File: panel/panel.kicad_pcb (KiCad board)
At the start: 2 copper layers, 80.9 x 128.5 mm, 4 parts

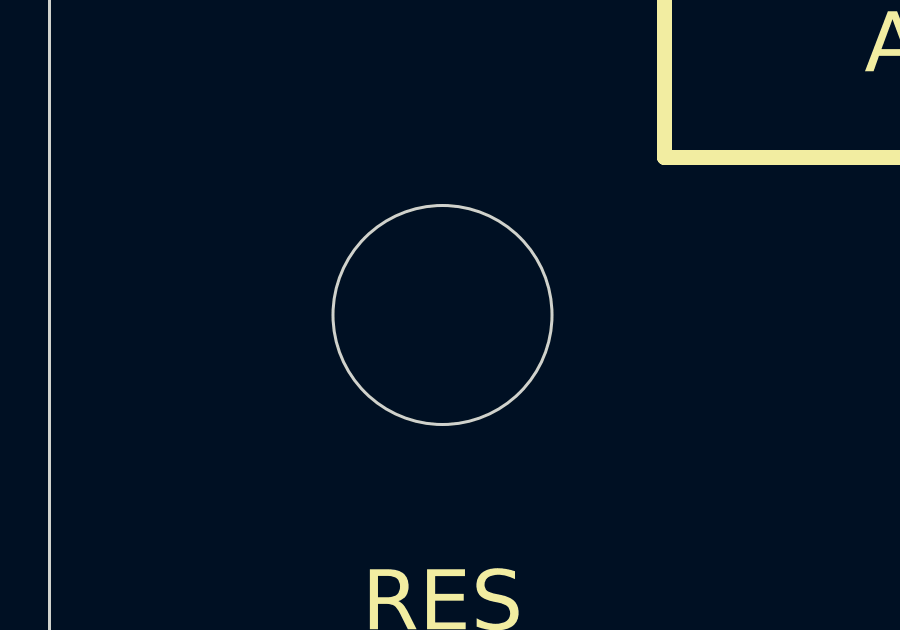
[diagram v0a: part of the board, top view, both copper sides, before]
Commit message: Added negative voltage protection diodes
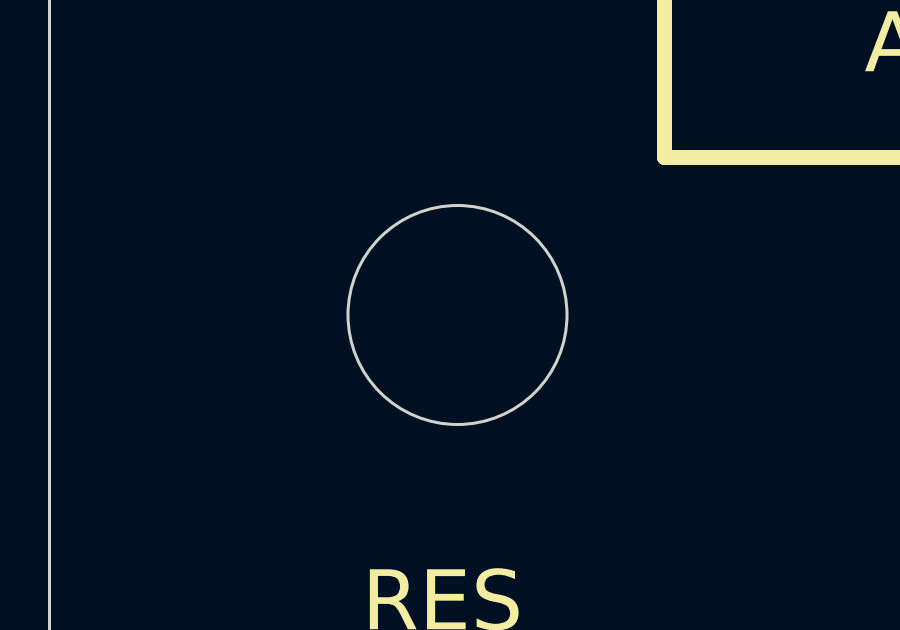
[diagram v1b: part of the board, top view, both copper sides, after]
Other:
- outline, holes or cut-outs redrawn
